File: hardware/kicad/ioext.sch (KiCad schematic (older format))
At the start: 46 parts, among them P1 CONN_01X04, P2 CONN_02X08, P3 CONN_01X10, Q1 IRLZ44N, Q2 IRLZ44N, Q3 IRLZ44N, Q4 IRLZ44N, Q5 IRLZ44N, Q6 IRLZ44N, Q7 IRLZ44N, Q8 IRLZ44N, U1 PCF8574A, U2 PC817, U3 PC817, U4 PC817, U5 PC817, U6 PC817, U7 PC817, U8 PC817, U9 PC817

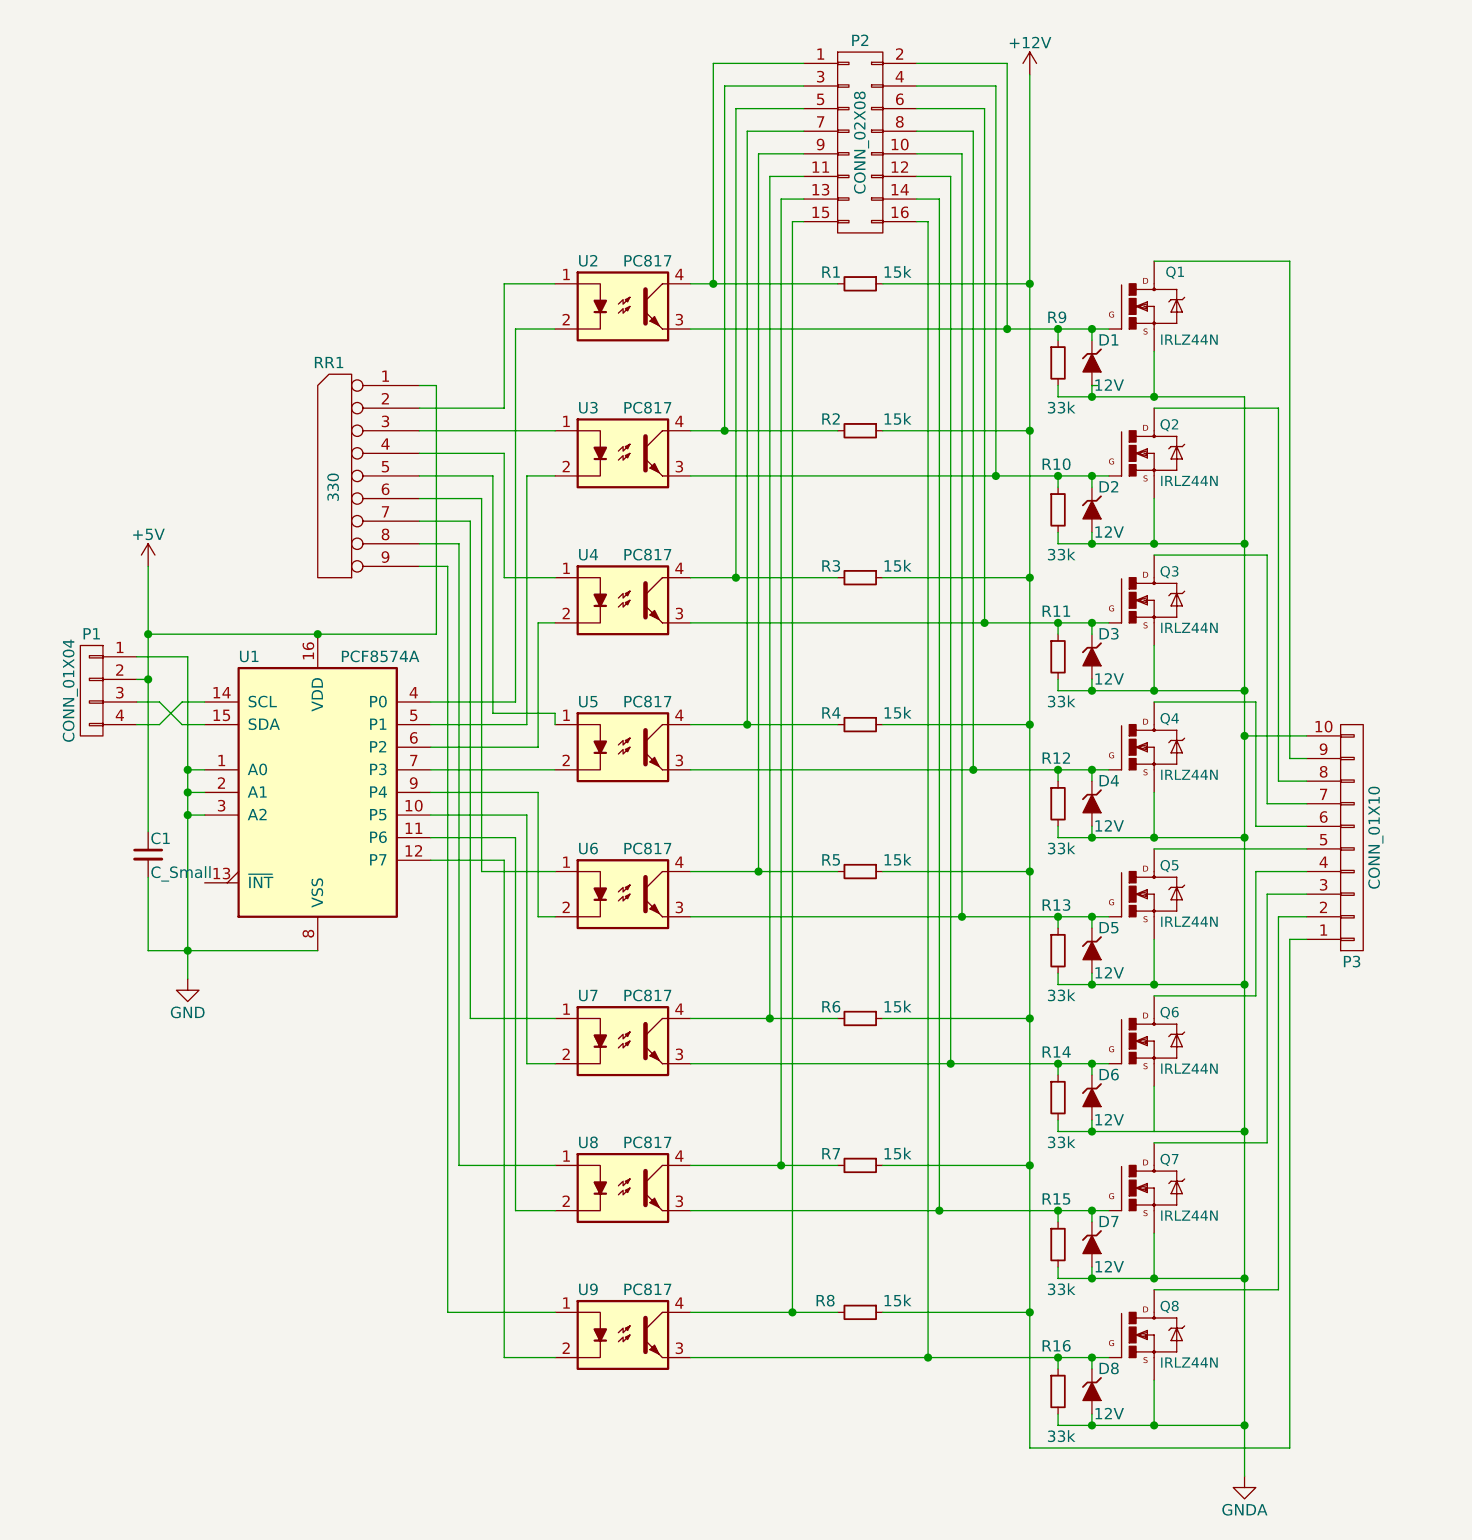
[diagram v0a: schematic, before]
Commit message: hardware/kicad ioext: use 3x jumper block insterad of inidividual jumpers
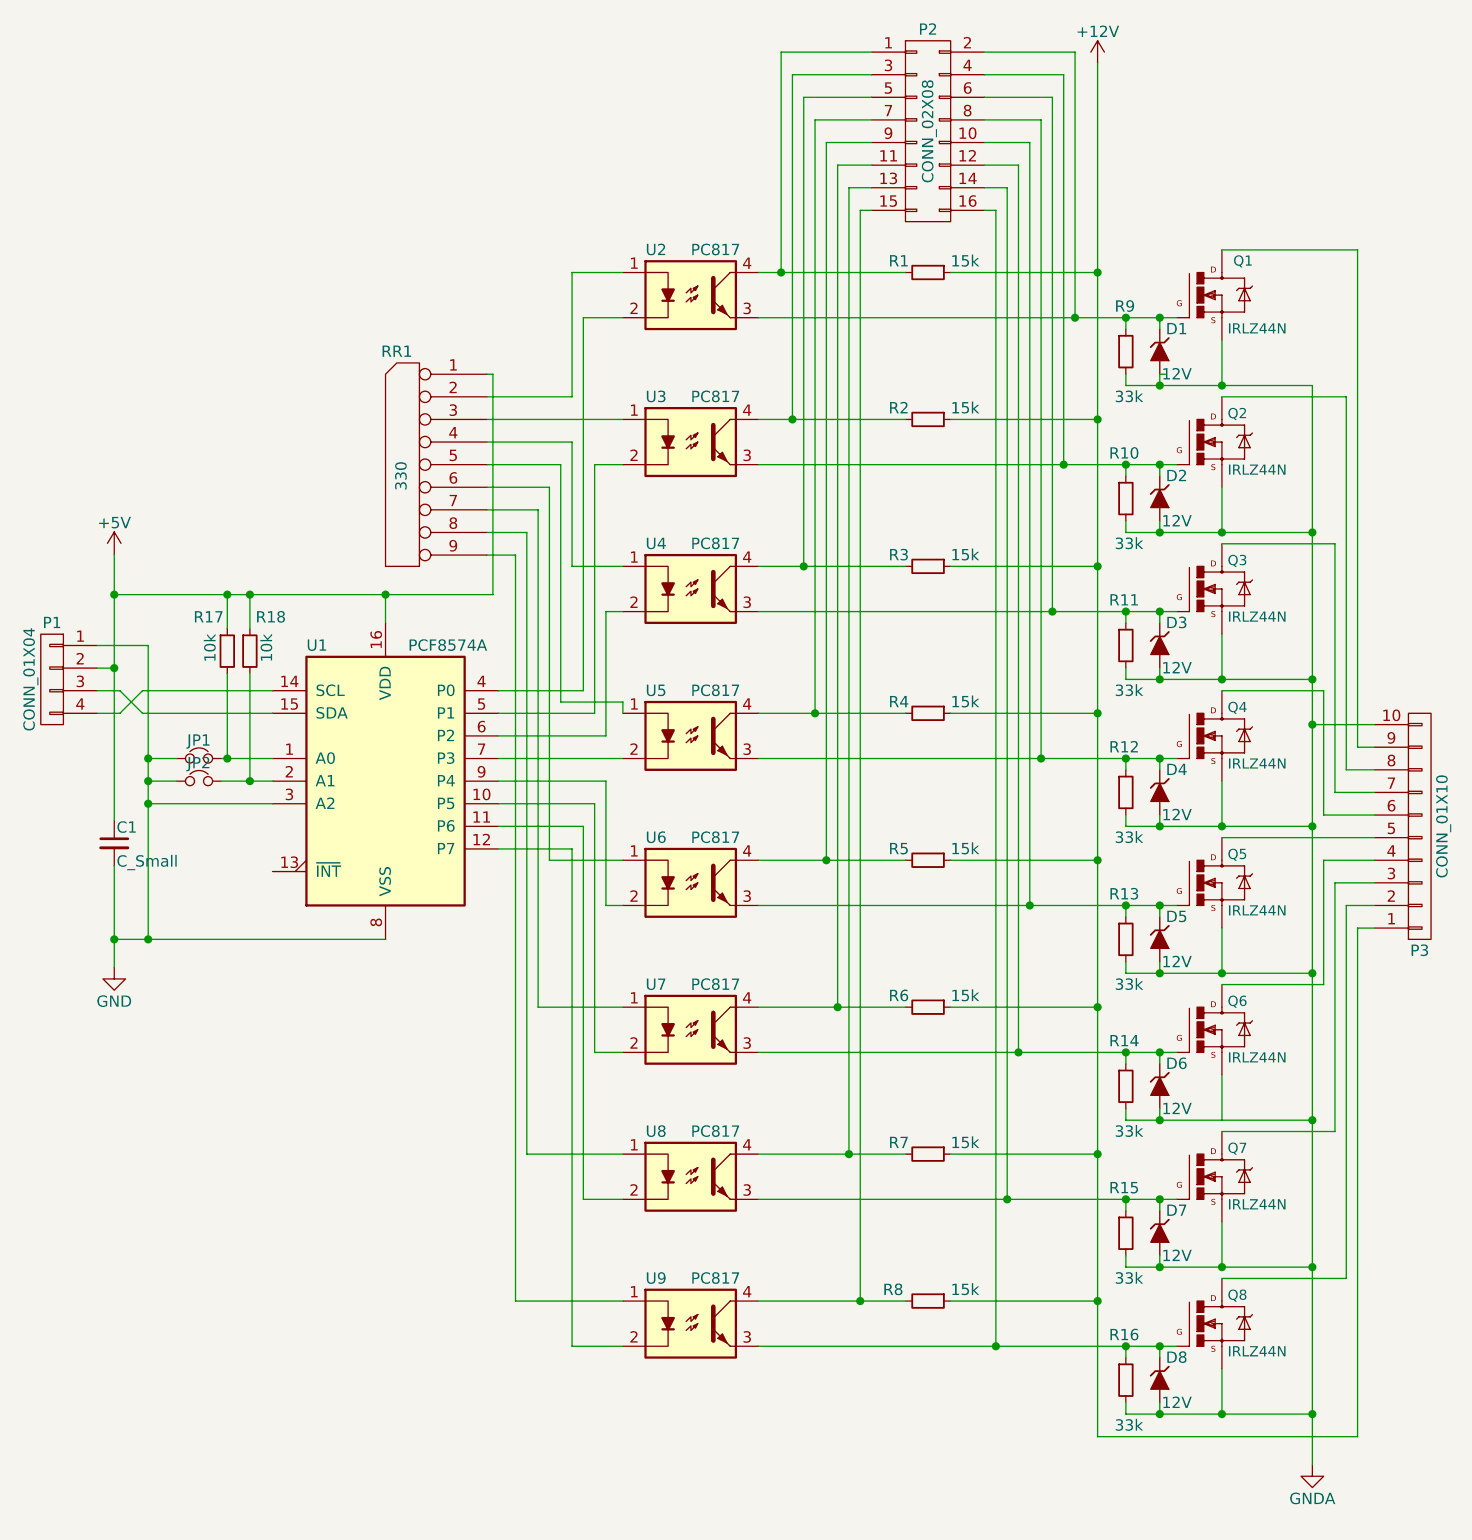
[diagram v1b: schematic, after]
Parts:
- added JP1, JP2: Jumper_NC_Small, Pin_Headers:Pin_Header_Straight_1x02, symbol Jumper_NC_Small
- added R17, R18: 10k, Resistors_SMD:R_0603_HandSoldering, symbol R_Small
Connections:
- net +5V: now also R17.1, R18.1
- net GND: now also JP1.1, JP2.1; no longer U1.1 (A0), U1.2 (A1)
- new net: JP1.2, R17.2, U1.1 (A0)
- new net: JP2.2, R18.2, U1.2 (A1)
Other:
- moved on the sheet: C1, D1, D2, D3, D4, D5, D6, D7, D8, P1, P2, P3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
